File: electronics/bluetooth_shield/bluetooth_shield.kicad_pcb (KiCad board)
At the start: 2 copper layers, 5 parts, among them IC1 453-00005, J1 Conn_02x08_Odd_Even, J2 Conn_01x03_Male, J3 Conn_01x04_Male, U1 AP2127R-3.3

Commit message: Updating layouts and schematics and reading for export
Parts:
- added C1: C, Capacitor_SMD:C_0805_2012Metric_Pad1.18x1.45mm_HandSolder, B.Cu at (39.4, 44.9)
- added H1: MountingHole, MountingHole:MountingHole_3.2mm_M3_DIN965_Pad_TopBottom, F.Cu at (46.6, 46.5)
- added H2: MountingHole, MountingHole:MountingHole_3.2mm_M3_DIN965_Pad_TopBottom, F.Cu at (46.5, 25.5)
- J2: value Conn_01x03_Male -> Conn_01x05_Male; footprint Connector_PinHeader_2.54mm:PinHeader_1x03_P2.54mm_Vertical -> Connector_PinHeader_2.54mm:PinHeader_1x05_P2.54mm_Vertical
- J3: value Conn_01x04_Male -> Conn_01x05_Male; footprint Connector_PinHeader_2.54mm:PinHeader_1x04_P2.54mm_Vertical -> Connector_PinHeader_2.54mm:PinHeader_1x05_P2.54mm_Vertical
- U1: moved to B.Cu
- moved J2 128.5 mm to (41.0, 39.6), turned to 270 degrees
- moved IC1 127.3 mm to (35.6, 29.2)
- moved J3 124.8 mm to (46.5, 30.9), turned to 0 degrees
- moved J1 115.4 mm to (23.9, 46.7), turned to 180 degrees
- moved U1 115.3 mm to (33.1, 45.5), turned to 270 degrees
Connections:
- IC1 pad 26: Net-(C1-Pad1) -> VDD
- J2 pad 1: Net-(IC1-Pad5) -> Net-(IC1-Pad17)
- J2 pad 2: Net-(IC1-Pad6) -> Net-(IC1-Pad18)
- J2 pad 3: Net-(IC1-Pad7) -> Net-(IC1-Pad19)
- J3 pad 1: Net-(IC1-Pad17) -> GND
- J3 pad 2: Net-(IC1-Pad18) -> Net-(IC1-Pad5)
- J3 pad 3: Net-(IC1-Pad19) -> Net-(IC1-Pad6)
- J3 pad 4: Net-(IC1-Pad20) -> Net-(IC1-Pad7)
- U1 pad 3: Net-(C1-Pad1) -> VDD
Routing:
- net MOSI: track 0.00 -> 25.7 mm, vias 0 -> 1
- net MISO: track 0.00 -> 24.9 mm, vias 0 -> 1
- net VDD: track 0.00 -> 21.9 mm, vias 0 -> 1
- net SDA: track 0.00 -> 16.0 mm
- net GND: track 0.00 -> 15.9 mm, vias 0 -> 8
- net SCL: track 0.00 -> 13.4 mm, vias 0 -> 1
- net +12V: track 0.00 -> 13.1 mm
- net Net-(IC1-Pad7): track 0.00 -> 12.5 mm
- net SCLK: track 0.00 -> 11.8 mm
- net Net-(IC1-Pad6): track 0.00 -> 10.7 mm
- net Net-(IC1-Pad5): track 0.00 -> 8.91 mm
- net Net-(IC1-Pad20): track 0.00 -> 5.49 mm
- net Net-(IC1-Pad19): track 0.00 -> 4.21 mm
- net Net-(IC1-Pad17): track 0.00 -> 4.15 mm
- net Net-(IC1-Pad18): track 0.00 -> 3.47 mm
- added copper zone on B.Cu, net GND
- added copper zone on F.Cu, net GND
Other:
- board outline added: 32.2 x 27.7 mm

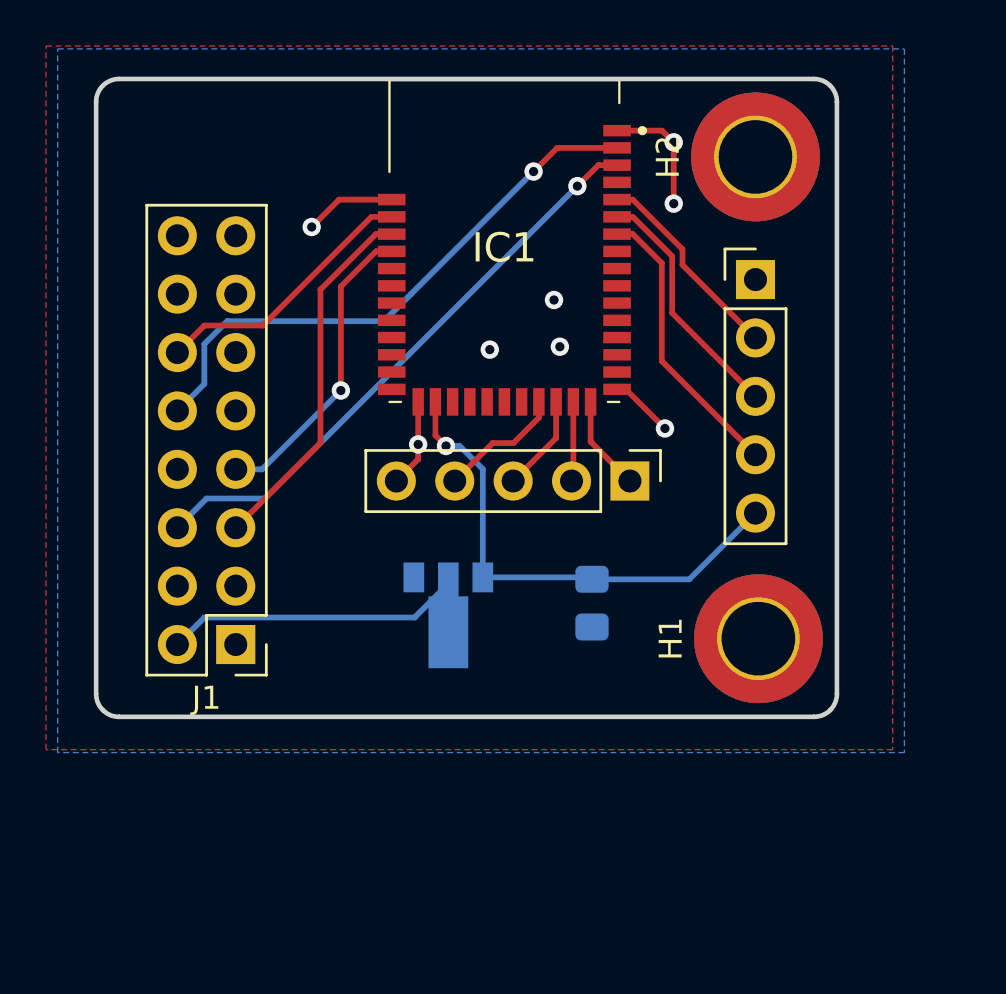
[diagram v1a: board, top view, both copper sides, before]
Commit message: Updating layouts for better shield addition
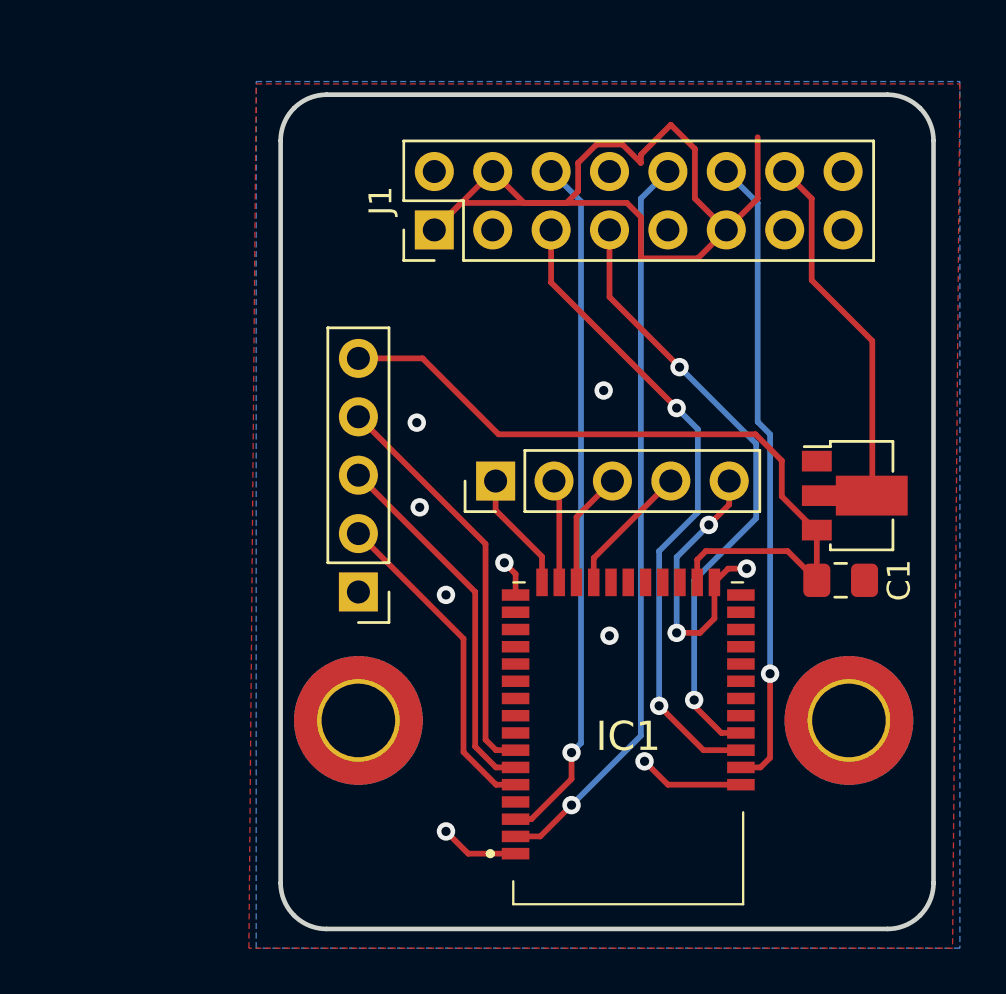
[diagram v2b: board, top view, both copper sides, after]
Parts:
- C1, U1: moved to F.Cu
- moved H2 30.0 mm to (29.2, 50.0)
- moved IC1 22.5 mm to (40.9, 51.0), turned to 180 degrees
- moved J3 22.0 mm to (29.2, 44.5), turned to 180 degrees
- moved J1 20.0 mm to (32.5, 28.7), turned to 90 degrees
- moved U1 18.4 mm to (50.8, 40.3), turned to 0 degrees
- moved C1 10.9 mm to (50.2, 43.9), turned to 0 degrees
- moved J2 5.84 mm to (35.2, 39.6), turned to 90 degrees
- moved H1 5.31 mm to (50.5, 50.0)
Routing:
- net GND: track 15.9 -> 63.1 mm, vias 8 -> 11
- net SCLK: track 11.8 -> 27.7 mm, vias 0 -> 1
- net SCL: track 13.4 -> 27.0 mm, vias 1 -> 2
- net SDA: track 16.0 -> 28.4 mm, vias 0 -> 2
- net VDD: track 21.9 -> 33.0 mm, vias 1 -> 0
- net MISO: track 24.9 -> 32.3 mm
- net Net-(IC1-Pad5): track 8.91 -> 14.3 mm
- net Net-(IC1-Pad7): track 12.5 -> 17.8 mm
- net Net-(IC1-Pad6): track 10.7 -> 16.0 mm
- net MOSI: track 25.7 -> 30.3 mm
- net +12V: track 13.1 -> 17.6 mm
- net Net-(IC1-Pad17): track 4.15 -> 5.24 mm
- net Net-(IC1-Pad18): track 3.47 -> 4.50 mm
- net Net-(IC1-Pad19): track 4.21 -> 5.06 mm
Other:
- board size 32.2 x 27.7 mm -> 28.4 x 36.3 mm
